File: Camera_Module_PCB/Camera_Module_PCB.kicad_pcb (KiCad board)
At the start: 4 copper layers, 110 parts, among them J1 SS-52400-002, J2 Conn_01x02, J3 FFC2A32-24-T, SW1 SW_DIP_x01, SW2 SW_Push, SW3 SW_Push, U2 ESP32-S3R8, U4 MAX98357AETE_T, U5 AP3032KTR-G1, Y1 40MHz

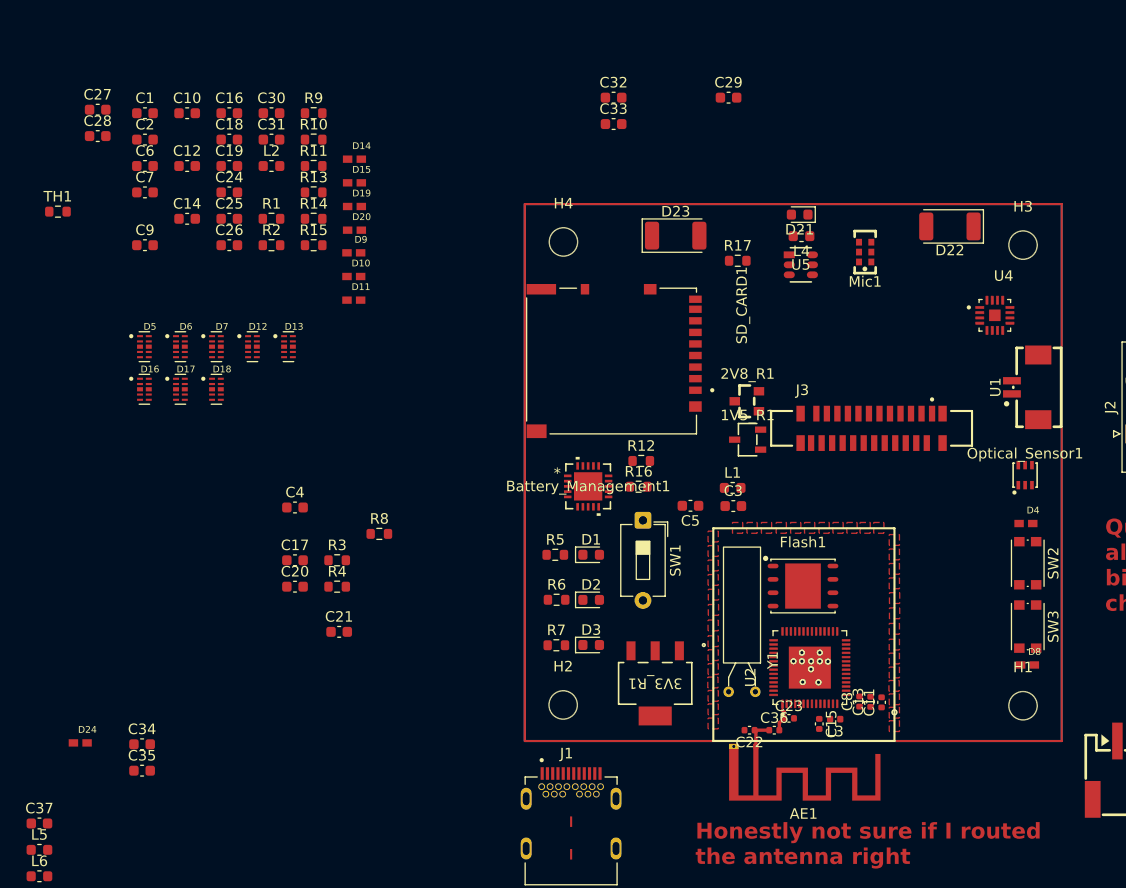
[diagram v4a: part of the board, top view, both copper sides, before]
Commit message: Continued to map out ESP32 Module portion of PCB
Continued to follow the Espressif PCB layout by routing power and placing general component location. The quartz crystal footprint was changed and the model we will be using replaced the value of the crystal in the schematic.
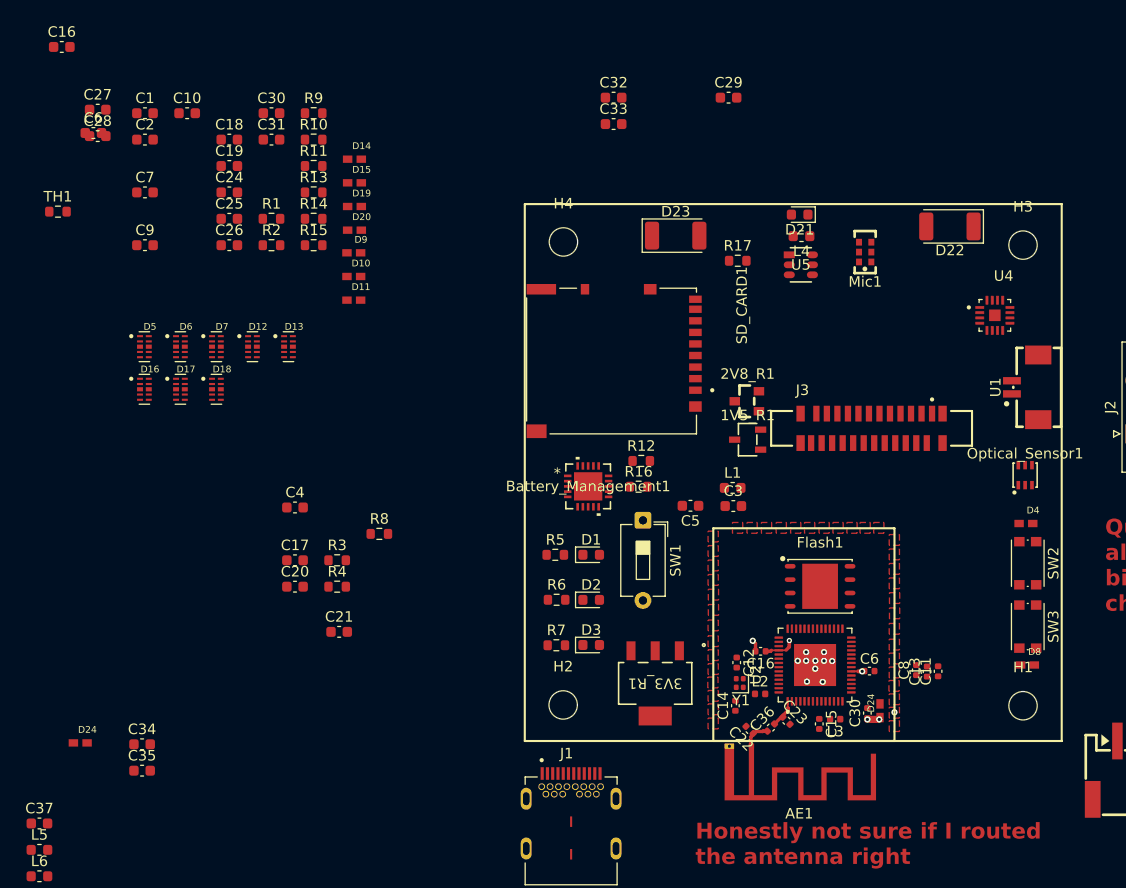
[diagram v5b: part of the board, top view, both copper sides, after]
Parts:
- added C16: 0.1uF, Capacitor_SMD:C_0402_1005Metric, F.Cu at (124.0, 93.3)
- added C30: 10uF, Capacitor_SMD:C_0402_1005Metric, F.Cu at (134.2, 99.2)
- added C6: 0.1uF, Capacitor_SMD:C_0402_1005Metric, F.Cu at (134.4, 95.2)
- added D24: 0402ESDA-MLP1, ESP32CAM_Foorprints:ESD_0402ESDA-MLP1, F.Cu at (135.4, 99.0)
- C12, C14: footprint Capacitor_SMD:C_0603_1608Metric -> Capacitor_SMD:C_0402_1005Metric
- L2: footprint Inductor_SMD:L_0603_1608Metric -> Inductor_SMD:L_0402_1005Metric
- Y1: value 40MHz -> Q40,0-JXS10-8-10/10-FU-LF1; footprint Crystal:Crystal_AT310_D3.0mm_L10.0mm_Horizontal -> Crystal:Crystal_SMD_1210-4Pin_1.2x1.0mm
- moved C12 70.4 mm to (121.8, 94.4), turned to -90 degrees
- moved C14 69.7 mm to (121.6, 98.5), turned to 90 degrees
- moved L2 68.4 mm to (124.0, 97.4)
- moved C16 17.1 mm to (57.6, 35.9)
- moved C8 6.17 mm to (138.8, 95.1)
- moved C11 6.13 mm to (140.9, 95.2)
- moved C13 6.10 mm to (139.8, 95.2)
- moved C6 5.82 mm to (60.6, 44.0)
- moved Y1 1.70 mm to (122.0, 96.3)
- moved Flash1 1.63 mm to (129.7, 87.1)
- moved U2 0.55 mm to (129.2, 94.6)
- moved AE1 0.43 mm to (123.2, 102.3)
- moved C36 0.41 mm to (125.0, 100.6), turned to 45 degrees
- moved C23 0.33 mm to (126.5, 99.9), turned to -45 degrees
- turned C22 to 135 degrees
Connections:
- AE1 pad 2: GND -> (no net)
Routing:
- net +3.3V: track 0.00 -> 25.5 mm, vias 1 -> 5
- net GND: track 0.00 -> 1.11 mm, vias 10 -> 11

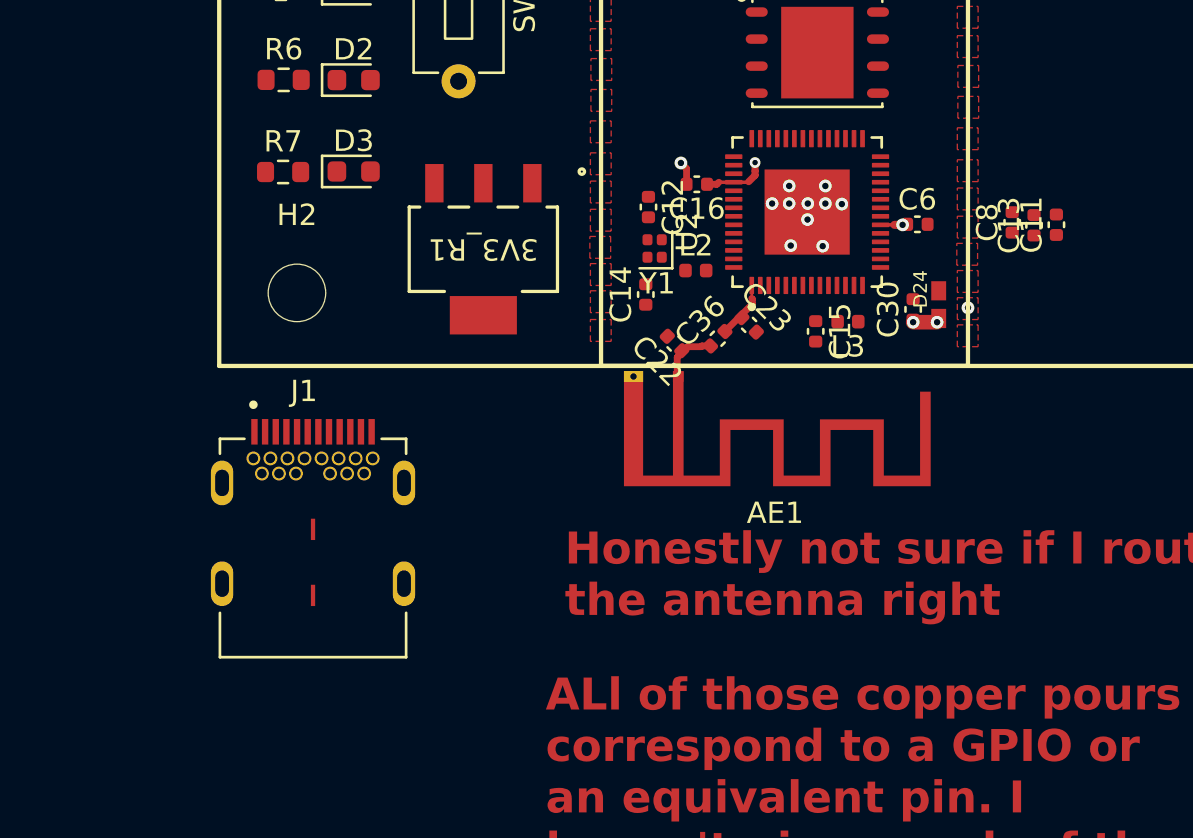
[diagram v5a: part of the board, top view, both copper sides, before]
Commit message: Made some schematic edits & continued work on layout
Made some minor adjustments for the schematic to prepare for review. The layout continues to be built.
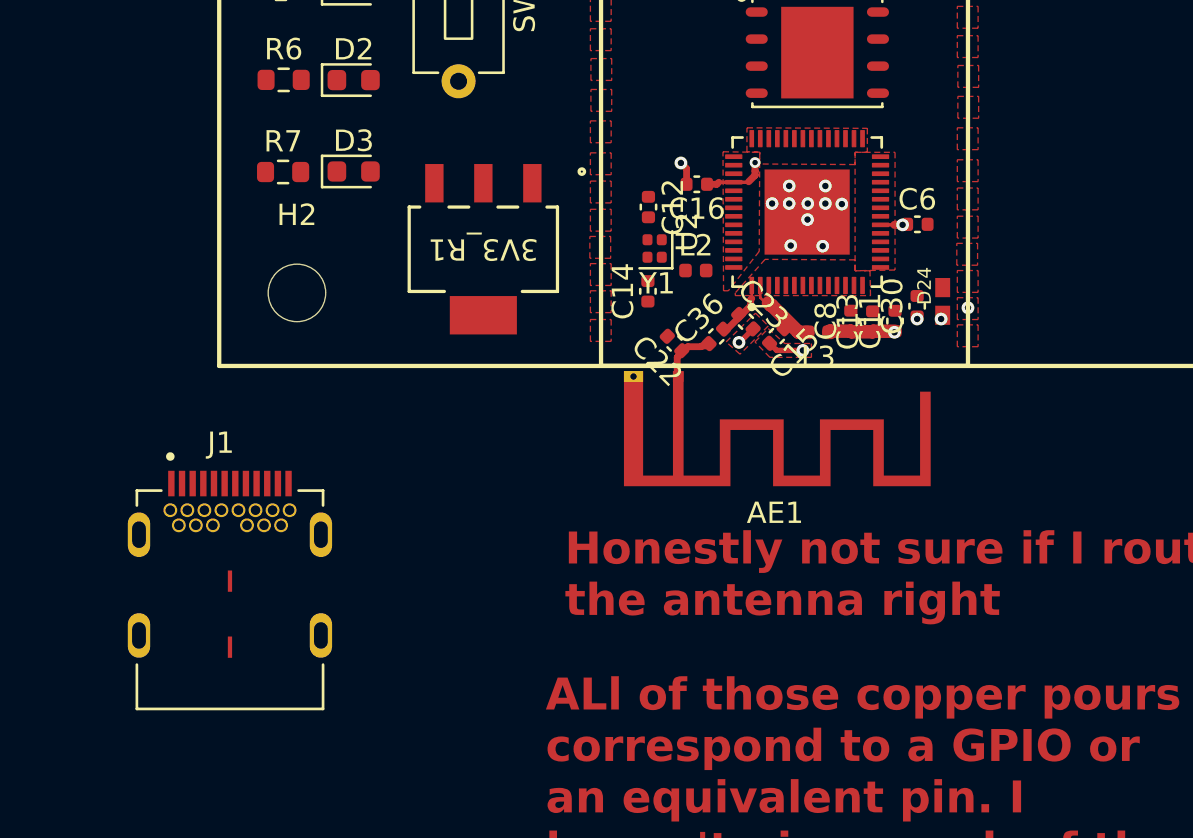
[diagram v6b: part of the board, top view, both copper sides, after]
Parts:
- moved C8 8.88 mm to (131.2, 99.7)
- moved C11 8.82 mm to (133.3, 99.7)
- moved C13 8.82 mm to (132.3, 99.8)
- moved J1 4.60 mm to (102.1, 114.5)
- moved C15 1.84 mm to (127.8, 100.5), turned to -135 degrees
- moved L3 1.48 mm to (129.7, 100.3)
- moved C30 0.24 mm to (134.4, 99.0)
- moved D24 0.24 mm to (135.6, 98.8)
- moved C23 0.21 mm to (126.3, 99.8)
- moved C14 0.18 mm to (121.7, 98.3)
- moved C36 0.13 mm to (124.9, 100.5)
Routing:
- net VDD3P3: track 0.00 -> 3.82 mm
- net GND: track 1.11 -> 3.74 mm, vias 11 -> 13
- net +3.3V: track 25.5 -> 28.1 mm, vias 5 -> 6
- added copper zone on F.Cu, net (none)

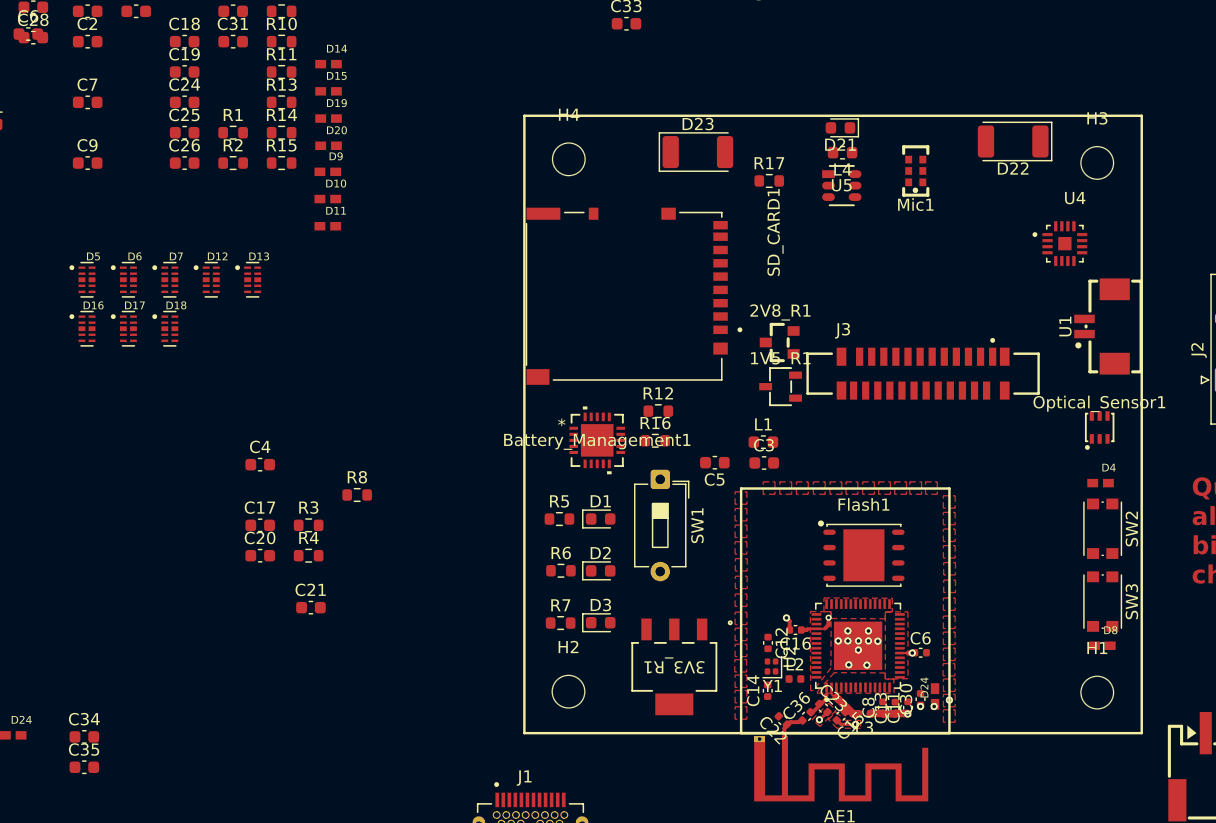
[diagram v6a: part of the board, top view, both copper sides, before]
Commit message: Routed Antenna and Crystal
The antenna and crystals that connect to the ESP32-S3 were routed and a dense layer of ground vias were used for isolation along with no net filled zones. There is a small concern between the RF trace and the 3V3 analog power at pins 2 and 3. Due to DRC, I am unable to place vias between then. Perhaps much smaller vias can be used as a compromise.
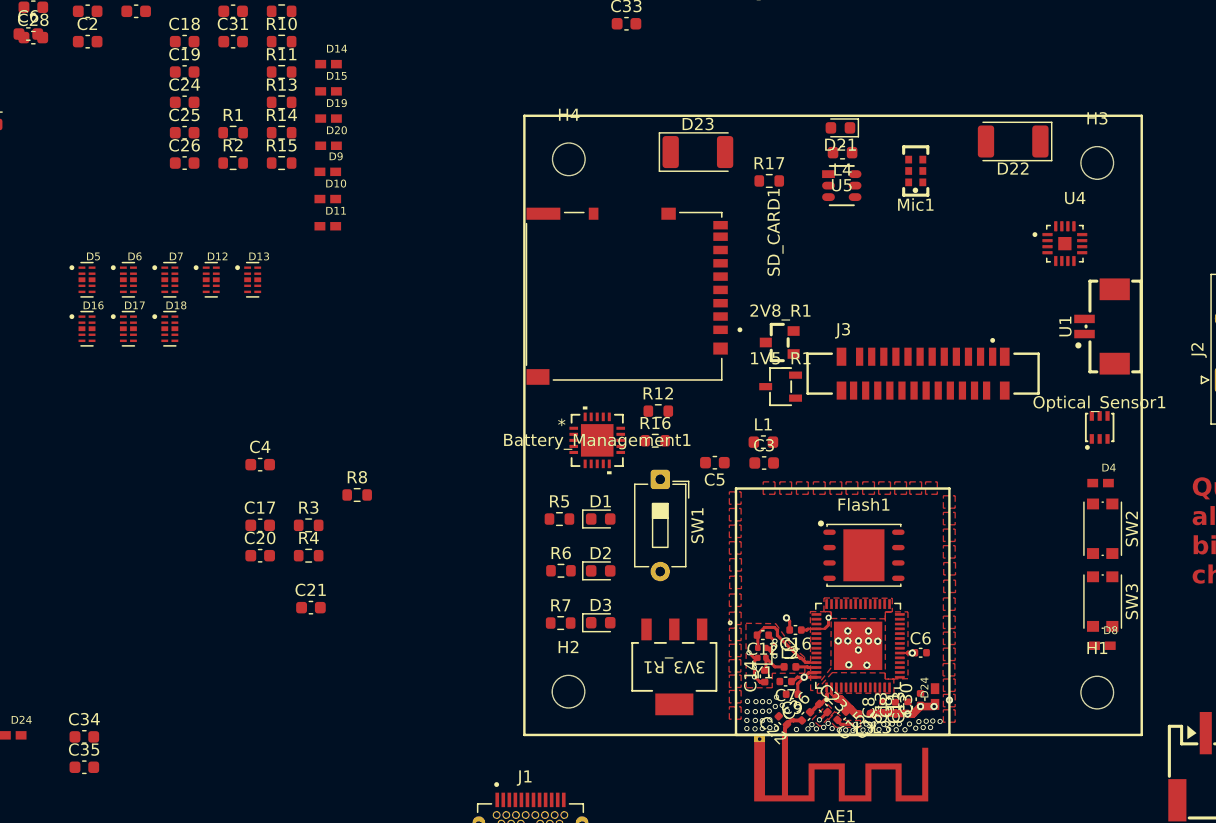
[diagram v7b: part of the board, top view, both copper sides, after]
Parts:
- C7, C9: footprint Capacitor_SMD:C_0603_1608Metric -> Capacitor_SMD:C_0402_1005Metric
- moved C7 75.0 mm to (123.2, 97.6), turned to 180 degrees
- moved C9 73.0 mm to (123.7, 98.6), turned to 180 degrees
- moved Y1 1.38 mm to (121.2, 95.2)
- moved C14 1.23 mm to (121.5, 97.2)
- moved L2 1.08 mm to (123.6, 96.4)
- moved C12 0.78 mm to (121.3, 93.8), turned to 180 degrees
- moved C15 0.07 mm to (127.8, 100.4)
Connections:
- Y1 pad 2: /XTAL_N -> GND
- Y1 pad 3: (no net) -> /XTAL_N
- Y1 pad 4: (no net) -> GND
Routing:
- net +3.3V: track 28.1 -> 43.7 mm, vias 6 -> 7
- net /XTAL_N: track 0.00 -> 7.86 mm
- net GND: track 3.74 -> 10.2 mm, vias 13 -> 69
- net Net-(Y1-Input): track 0.00 -> 2.90 mm
- net /XTAL_P: track 0.00 -> 1.73 mm
- net Net-(AE1-A): track 2.61 -> 1.55 mm
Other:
- board text added: "C13"
- board text added: "C15"
- board text added: "C8"
- board text added: "L3"
